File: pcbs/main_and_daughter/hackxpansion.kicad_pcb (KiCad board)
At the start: 4 copper layers, 52 x 69 mm, 97 parts, among them CN1 533981471, CN2 533981471, CN3 533981471, CN4 533981471, IC1 ADS7128IRTET, J1 Conn_01x03_MountingPin, J2 USB_C_Receptacle_USB2.0_14P, Q1 BSS138, Q2 2N7002, SW1 SW_Push, SW2 SW_Push, SW3 SW_On_Off, U2 RP2354B, U5 SPX3819M5-L-3-3, U7 BQ24075RGT, U8 USBLC6-2SC6, Y1 ABM8-272-T3

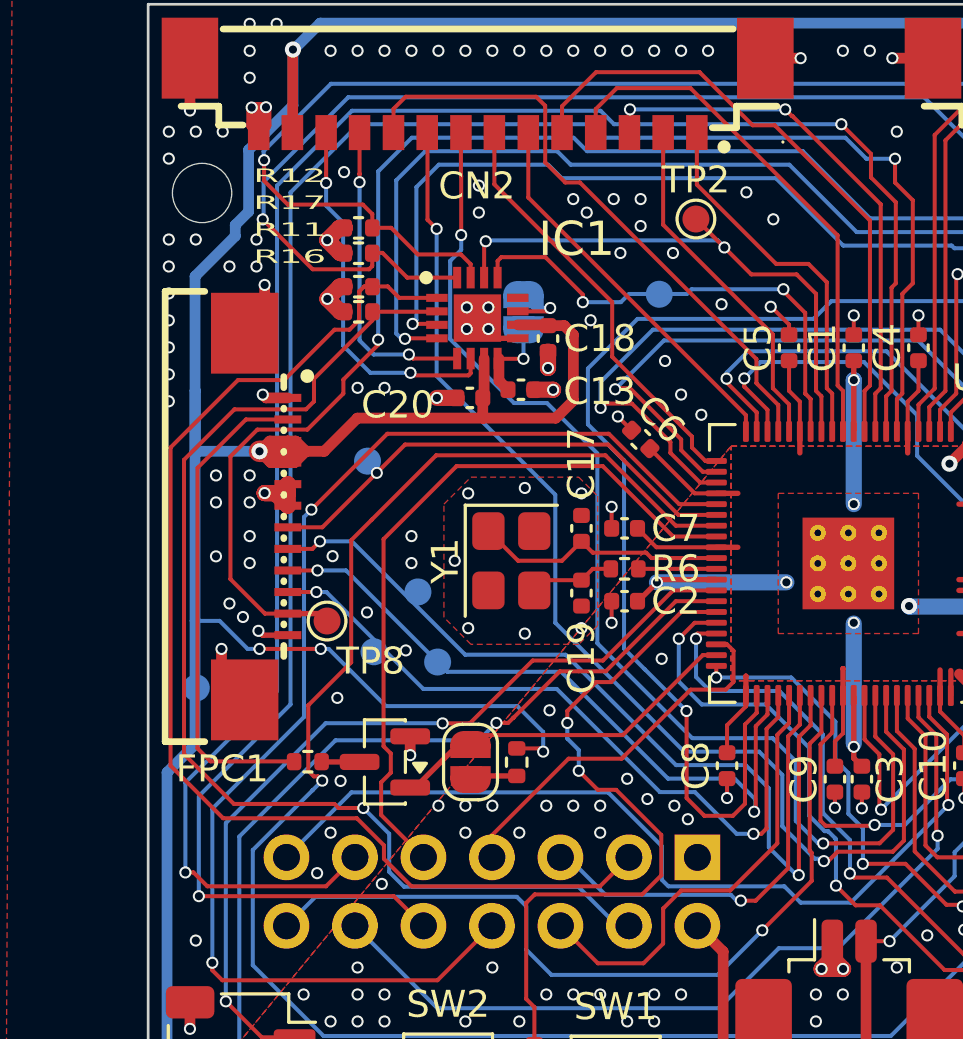
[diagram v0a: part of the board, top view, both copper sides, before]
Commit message: moved display connector up 1.6mm
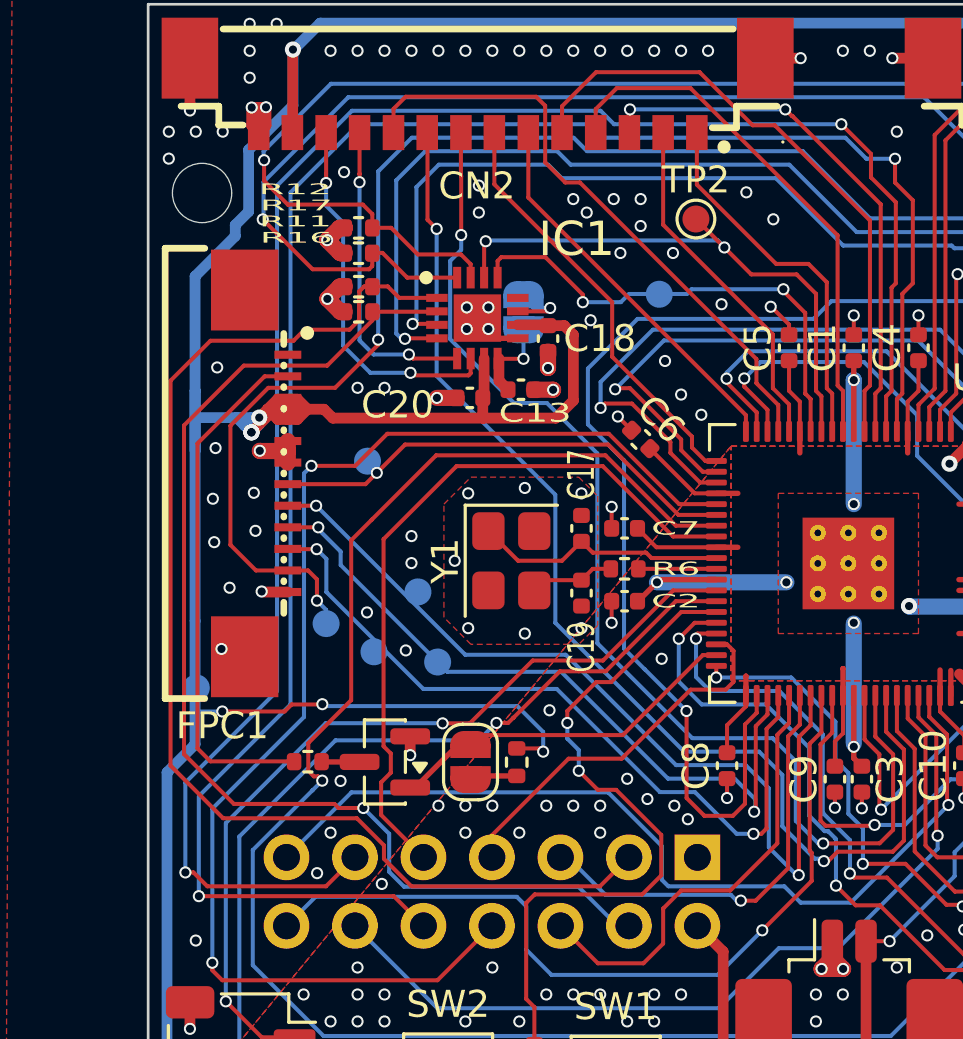
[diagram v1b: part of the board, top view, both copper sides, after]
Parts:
- TP8: moved to B.Cu
- moved FPC1 1.60 mm to (106.2, 75.3)
- moved TP8 0.10 mm to (108.5, 80.9)
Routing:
- net /GND: track 66.9 -> 60.6 mm, vias 378 -> 361
- net /Main Board/ADC/mod0.MD0: track 44.5 -> 46.0 mm
- net /Main Board/Display/MOSI: track 26.7 -> 28.1 mm
- net /+3V3: track 301.3 -> 302.7 mm, vias 13 -> 15
- net Net-(FPC1-Pad2): track 18.3 -> 19.5 mm
- net /Main Board/Display/SCLK: track 25.9 -> 26.8 mm
- net /Main Board/Module Bay 0/GPIO3: track 47.2 -> 48.2 mm
- net /Main Board/Display/DC: track 18.8 -> 18.2 mm
- net /Main Board/Display/RESET: track 56.2 -> 56.6 mm, vias 2 -> 3
